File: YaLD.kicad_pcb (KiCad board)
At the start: 2 copper layers, 99.1 x 72.4 mm, 89 parts, among them IC1 ATMEGA32-A, IC2 PCA9685, IC3 PCA9685, J1 RJDMXin, J2 RJDMXout, K1 IR_RCV, K2 DMXin, K3 DMXout, P1 PWR_IN, P10 CONN_01X04, P11 CONN_01X04, P12 CONN_01X04, P13 CONN_01X04, P14 CONN_01X02, P2 ISP, P3 CONN_01X02, P4 CONN_01X04, P5 CONN_01X04, P6 CONN_01X04, P7 CONN_01X04, P8 CONN_01X04, P9 CONN_01X04, SW1 DIPS_10, U1 75LBC176, U10 IRF7103, U11 IRF7103, U12 IRF7103, U13 IRF7103, U14 IRF7103, U15 IRF7103, U16 IRF7103, U17 IRF7103, U18 IRF7103, U2 7805_f, U3 IRF7103, U4 IRF7103, U5 IRF7103, U6 IRF7103, U7 IRF7103, U8 IRF7103, U9 IRF7103, X1 16MHz

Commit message: added debug connector (software UART TX)
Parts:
- added P15: DEBUG, Pin_Headers:Pin_Header_Straight_1x02, F.Cu at (58.7, 79.7)
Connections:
- IC1 pad 22: Net-(IC1-Pad22) -> DEBUG_TXD
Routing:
- net DEBUG_TXD: track 0.00 -> 4.02 mm
- net GND: track 130.5 -> 132.8 mm, vias 33 -> 34
- net VCC: track 261.6 -> 263.8 mm
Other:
- board text added: "Debug"

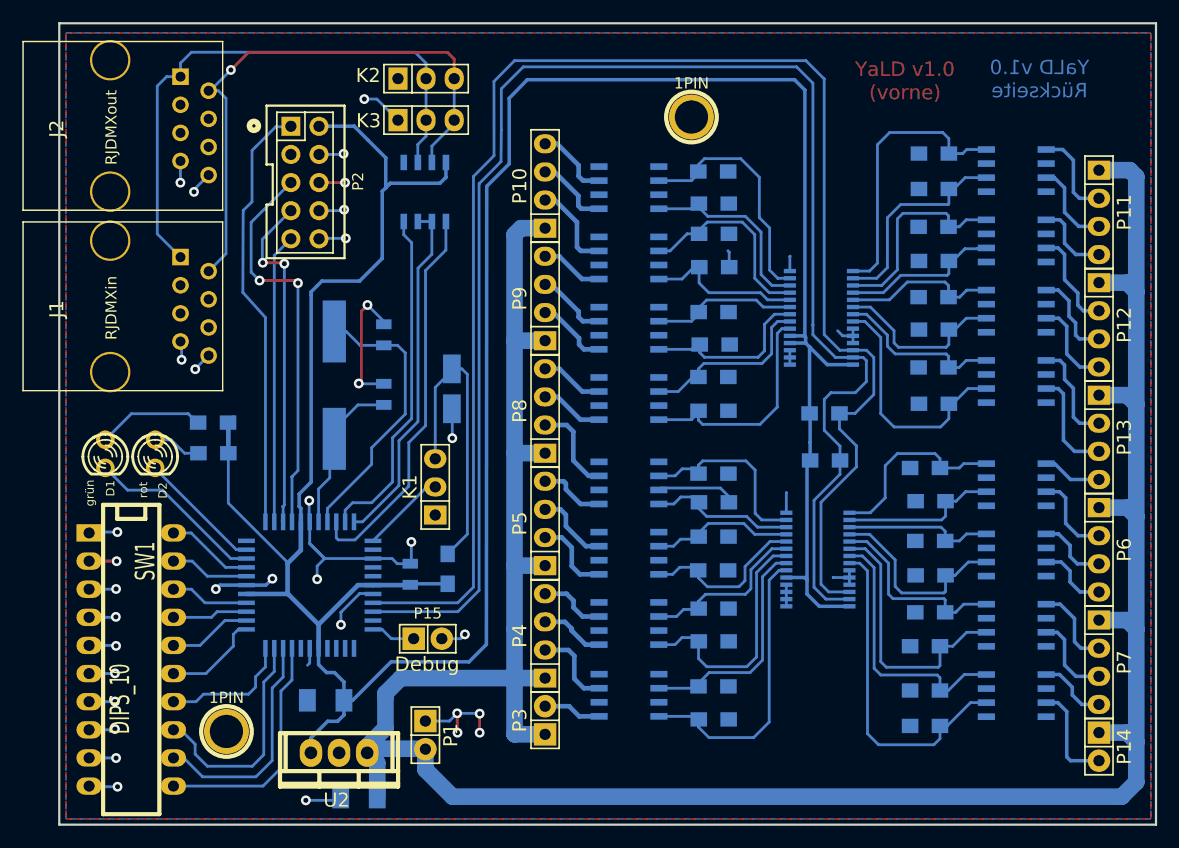
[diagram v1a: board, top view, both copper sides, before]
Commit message: changed outputs to 3.5mm pitch
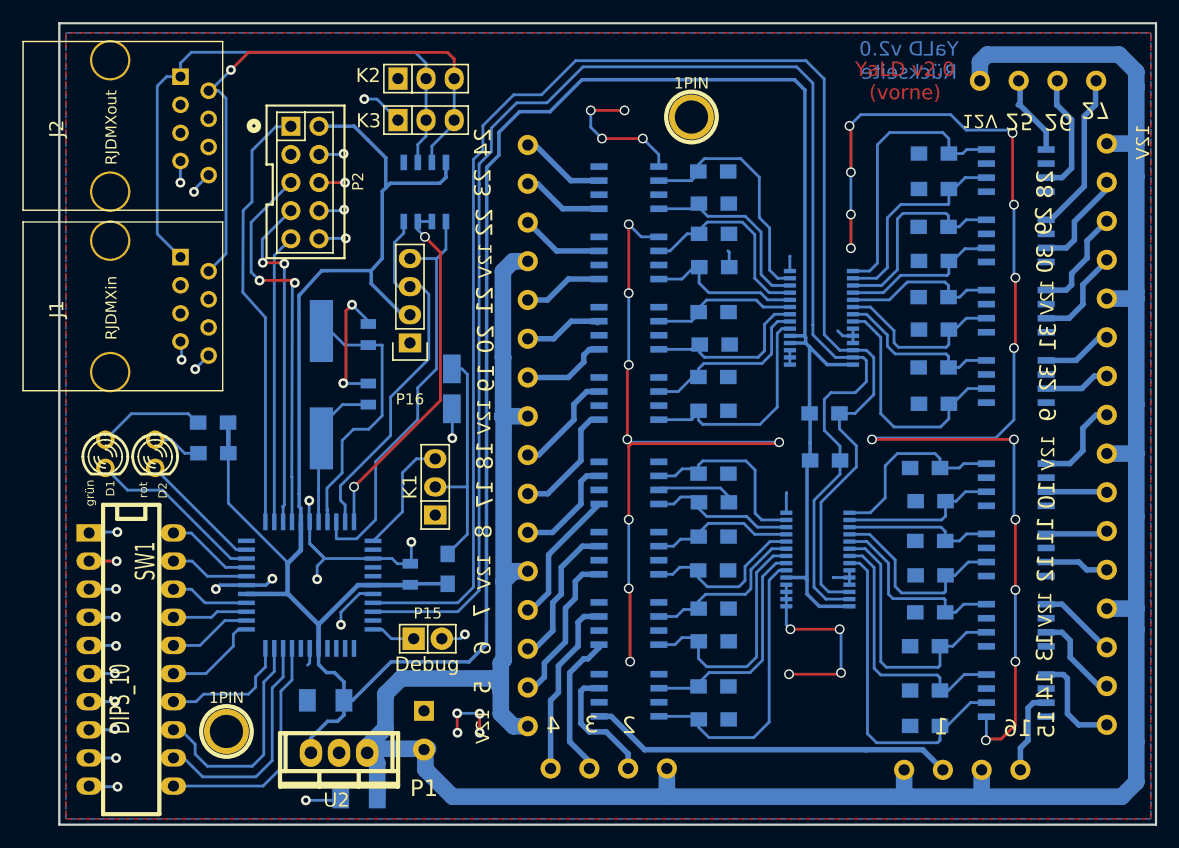
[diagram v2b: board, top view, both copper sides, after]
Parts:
- removed P14: CONN_01X02, Pin_Headers:Pin_Header_Straight_1x02
- added P16: UART, Pin_Headers:Pin_Header_Straight_1x04, F.Cu at (57.1, 53.0)
- P1: footprint Pin_Headers:Pin_Header_Straight_1x02 -> CONN_1_4_Pitch_3_5:CONN_1_2_Pitch_3_5
- P10, P11, P12, P13, P4, P5, P6, P7, P8, P9: footprint Pin_Headers:Pin_Header_Straight_1x04 -> CONN_1_4_Pitch_3_5:CONN_1_4_XY350_Pitch_3.5
- P3: value CONN_01X02 -> CONN_01X04; footprint Pin_Headers:Pin_Header_Straight_1x02 -> CONN_1_4_Pitch_3_5:CONN_1_4_XY350_Pitch_3.5
- moved P3 39.7 mm to (108.7, 91.6)
- moved P4 12.6 mm to (73.3, 91.4), turned to 270 degrees
- moved P11 12.5 mm to (115.6, 29.3), turned to 90 degrees
- moved P5 11.4 mm to (67.7, 80.6), turned to 180 degrees
- moved P12 9.40 mm to (120.0, 42.0), turned to 0 degrees
- moved P8 7.64 mm to (67.7, 66.6), turned to 180 degrees
- moved P13 5.57 mm to (120.0, 56.0), turned to 0 degrees
- moved P9 3.96 mm to (67.7, 52.6), turned to 180 degrees
- moved P7 2.26 mm to (120.0, 84.0), turned to 0 degrees
- moved P6 1.83 mm to (120.0, 70.0), turned to 0 degrees
- moved P10 1.58 mm to (67.7, 38.6), turned to 180 degrees
- moved C2 1.40 mm to (53.3, 52.2)
- moved C1 1.40 mm to (53.3, 57.6)
- moved P1 1.31 mm to (58.3, 89.7), turned to 0 degrees
- moved X1 1.17 mm to (49.1, 56.8)
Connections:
- K1 pad 2: INT1 -> Net-(C3-Pad1)
- K1 pad 3: Net-(C3-Pad1) -> INT1
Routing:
- net GND: track 132.8 -> 332.9 mm, vias 34 -> 60
- net OUT0: track 5.26 -> 33.1 mm
- net OUT3: track 6.08 -> 16.3 mm
- net 12V: track 235.4 -> 245.5 mm
- net OUT2: track 5.83 -> 13.5 mm
- net OUT26: track 7.06 -> 14.7 mm
- net OUT4: track 7.24 -> 14.1 mm
- net OUT6: track 6.03 -> 12.4 mm
- net OUT5: track 6.85 -> 13.2 mm
- net (no net): track 0.00 -> 5.66 mm, vias 0 -> 4
- net OUT16: track 5.72 -> 10.8 mm
- net VCC: track 263.8 -> 268.9 mm
- net Net-(C3-Pad1): track 27.7 -> 23.3 mm
- net OUT25: track 7.88 -> 11.9 mm
- net OUT17: track 5.72 -> 9.63 mm
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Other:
- board text added: "1"
- board text added: "10"
- board text added: "11"
- board text added: "12"
- board text added: "12V"
- board text added: "13"
- board text added: "14"
- board text added: "15"
- board text added: "16"
- board text added: "17"
- board text added: "18"
- board text added: "19"
- board text added: "2"
- board text added: "20"
- board text added: "21"
- board text added: "22"
- board text added: "23"
- board text added: "24"
- board text added: "25"
- board text added: "26"
- board text added: "27"
- board text added: "28"
- board text added: "29"
- board text added: "3"
- board text added: "30"
- board text added: "31"
- board text added: "32"
- board text added: "4"
- board text added: "5"
- board text added: "6"
- board text added: "7"
- board text added: "8"
- board text added: "9"
- board text added: "YaLD v2.0 (vorne)"
- board text added: "YaLD v2.0 Rückseite"
- board text removed: "YaLD v1.0 (vorne)"
- board text removed: "YaLD v1.0 Rückseite"

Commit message: added silk texts, corrected bugs
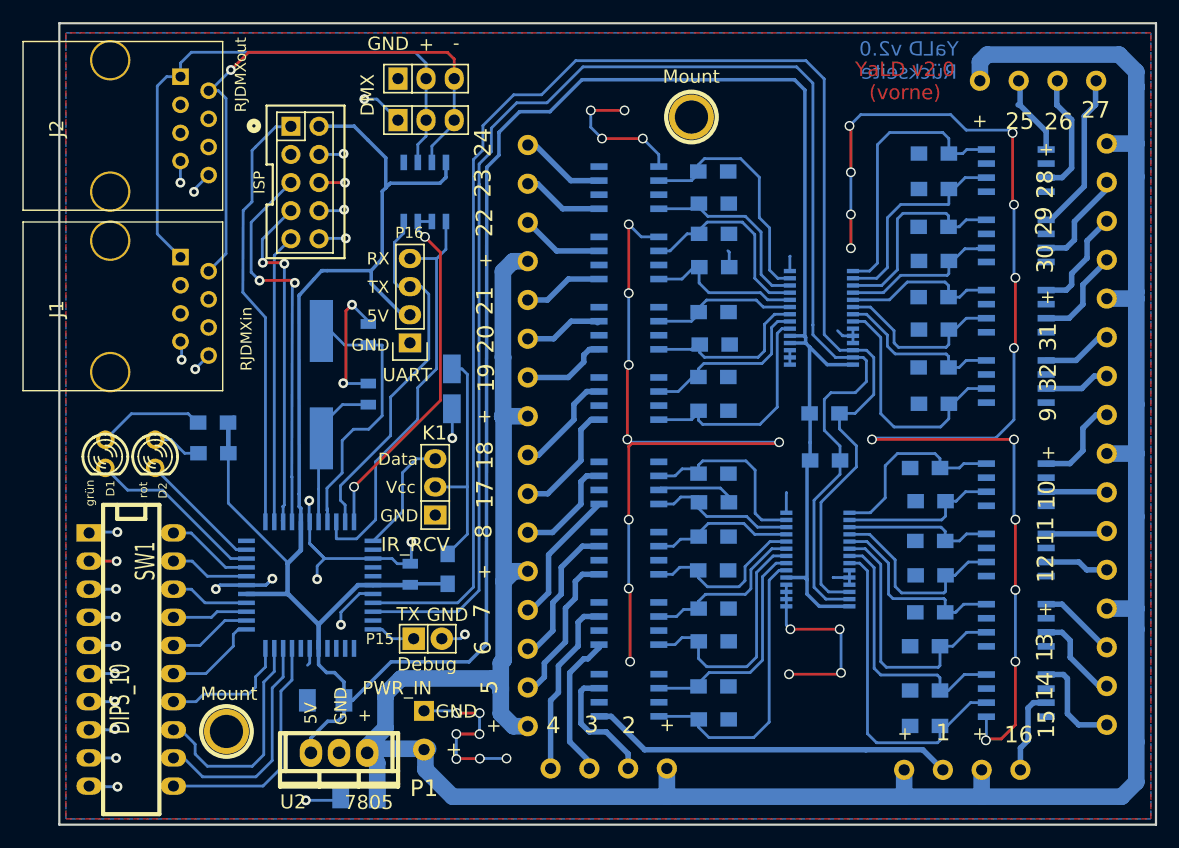
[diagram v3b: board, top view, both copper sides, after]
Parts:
- U2: value 7805_f -> 7805
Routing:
- net GND: track 332.9 -> 348.9 mm, vias 60 -> 67
- net (no net): track 5.66 -> 0.00 mm, vias 4 -> 0
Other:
- board text added: "+"
- board text added: "-"
- board text added: "5V"
- board text added: "DMX"
- board text added: "Data"
- board text added: "GND"
- board text added: "Mount"
- board text added: "RX"
- board text added: "TX"
- board text added: "Vcc"
- board text removed: "12V"

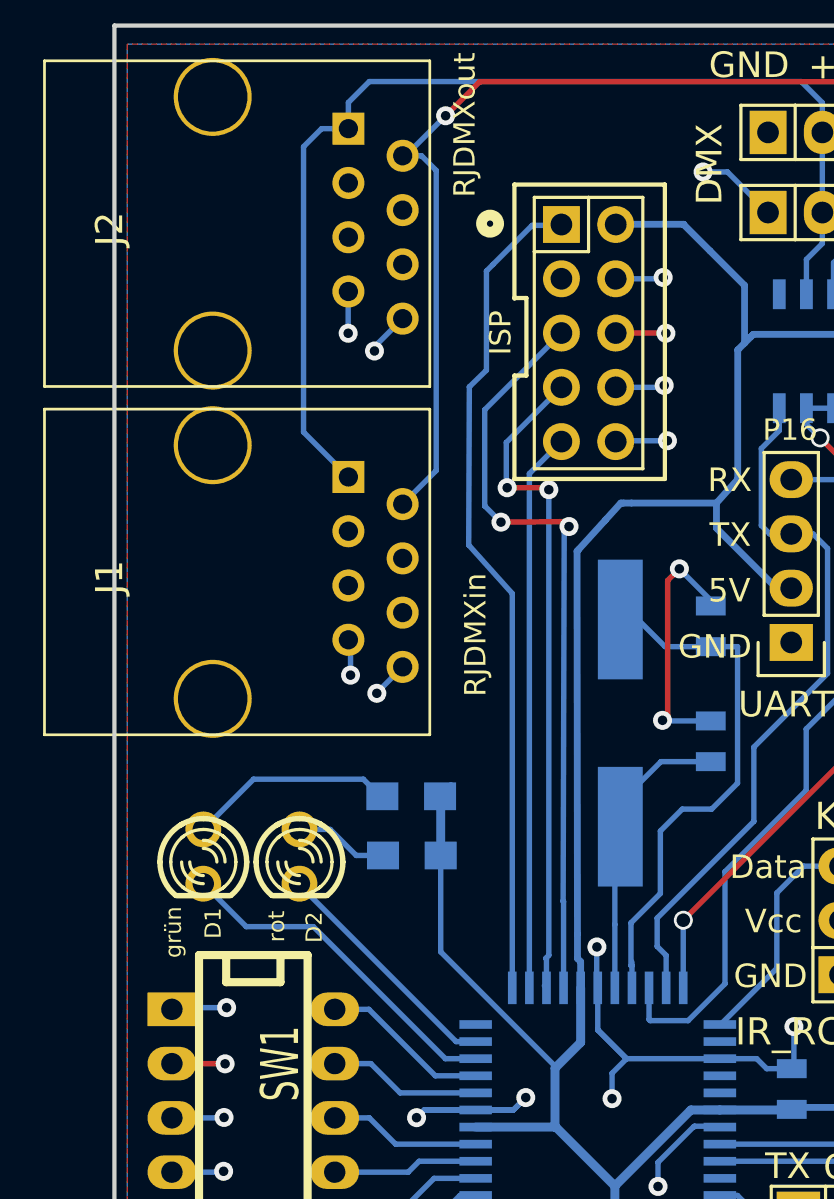
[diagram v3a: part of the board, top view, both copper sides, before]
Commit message: moved rj45
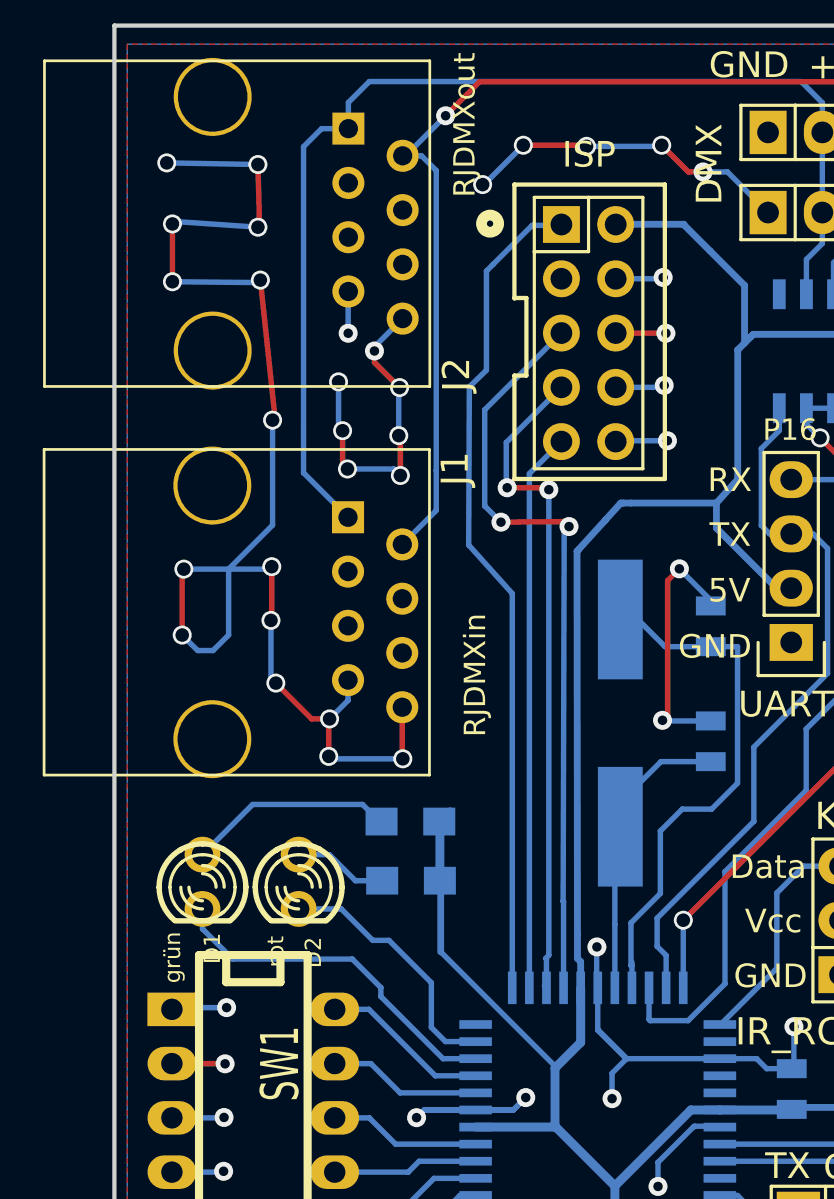
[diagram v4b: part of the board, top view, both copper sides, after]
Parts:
- moved J1 1.89 mm to (30.0, 51.6)
- moved R1 1.18 mm to (39.3, 61.4)
- moved R2 1.18 mm to (39.3, 64.2)
- moved D1 1.18 mm to (29.5, 64.2)
- moved D2 1.18 mm to (34.0, 64.2)
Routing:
- net GND: track 348.9 -> 434.7 mm, vias 67 -> 90
- net DMXminus: track 53.1 -> 55.0 mm
- net DMXplus: track 52.3 -> 54.1 mm
- net VCC: track 268.9 -> 267.8 mm
- net LEDgreen: track 16.1 -> 17.0 mm
- net LEDred: track 11.3 -> 12.1 mm
